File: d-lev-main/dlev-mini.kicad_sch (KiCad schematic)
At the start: 28 parts, among them J1 IO_BOARD, J3 S8B-PH-SM4-TB, J4 S8B-PH-SM4-TB, J6 S6B-PH-SM4-TB, Q1 MMBT3904, U2 AMS1117-3.3

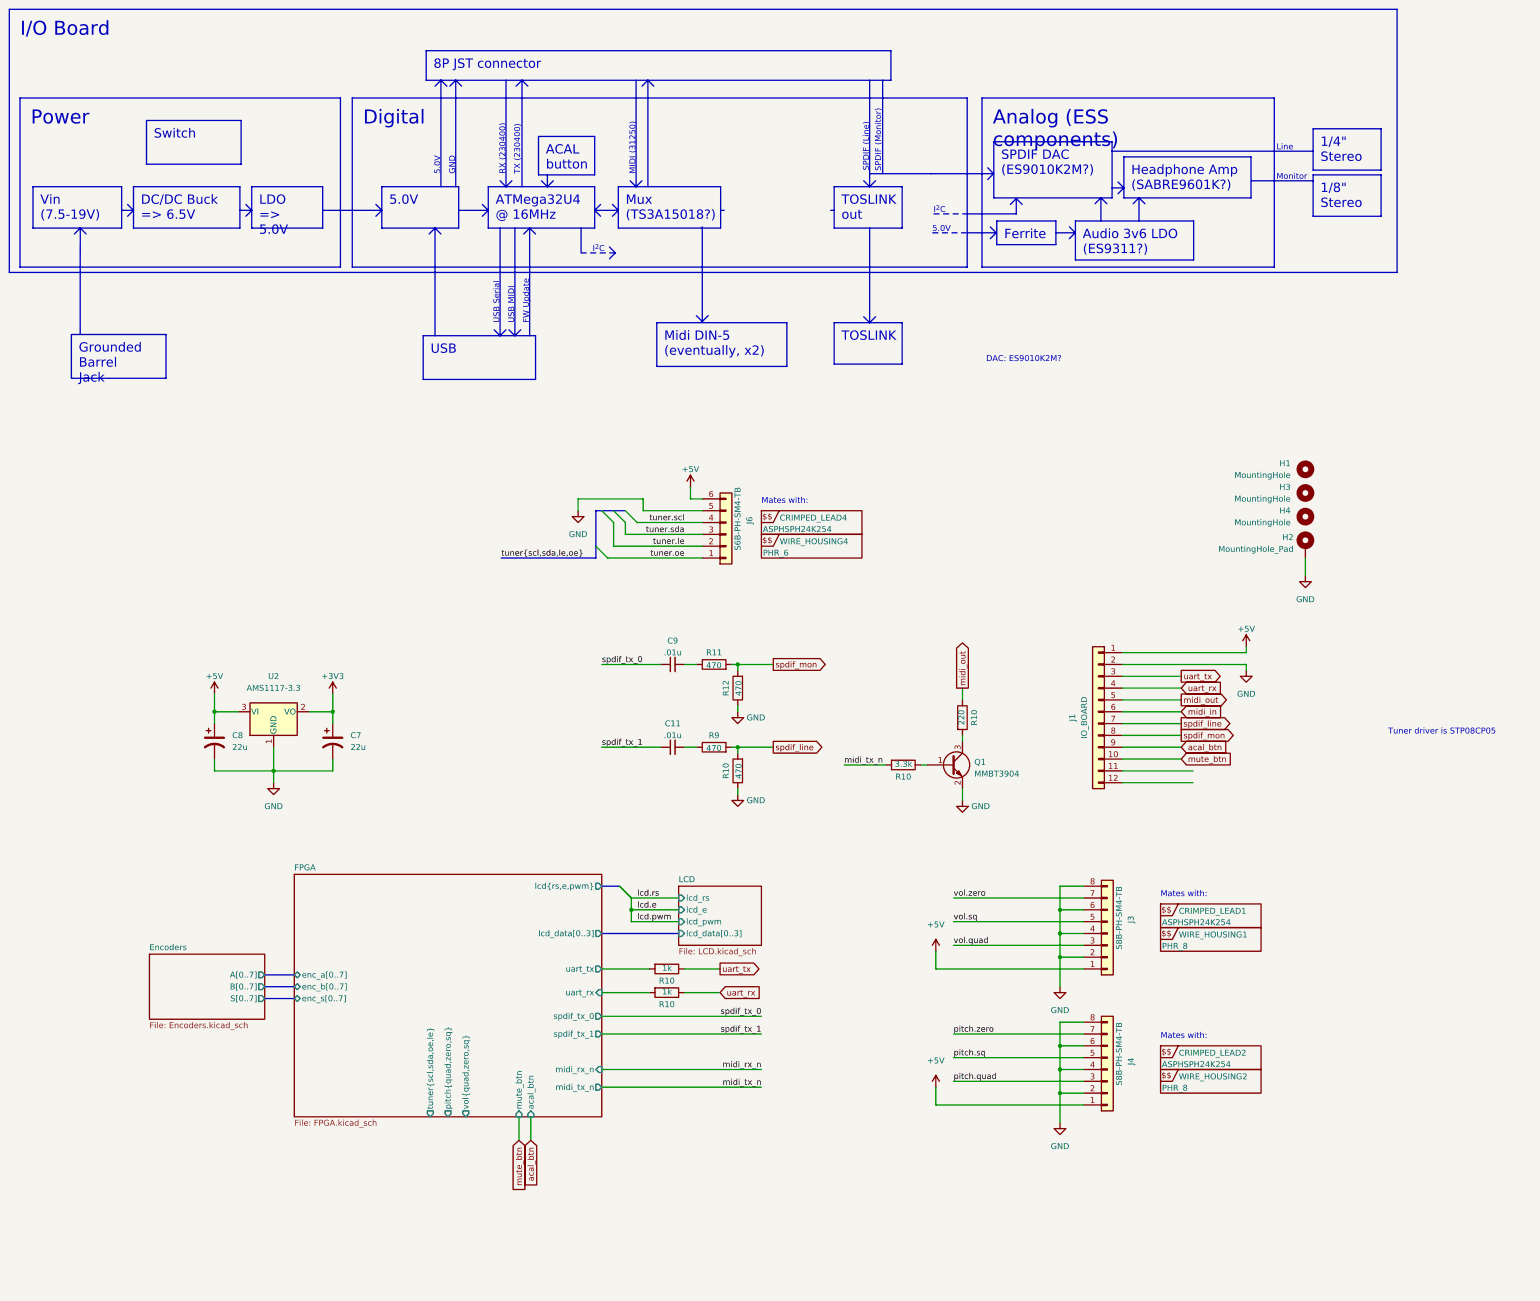
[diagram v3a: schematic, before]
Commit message: clean up 3d models
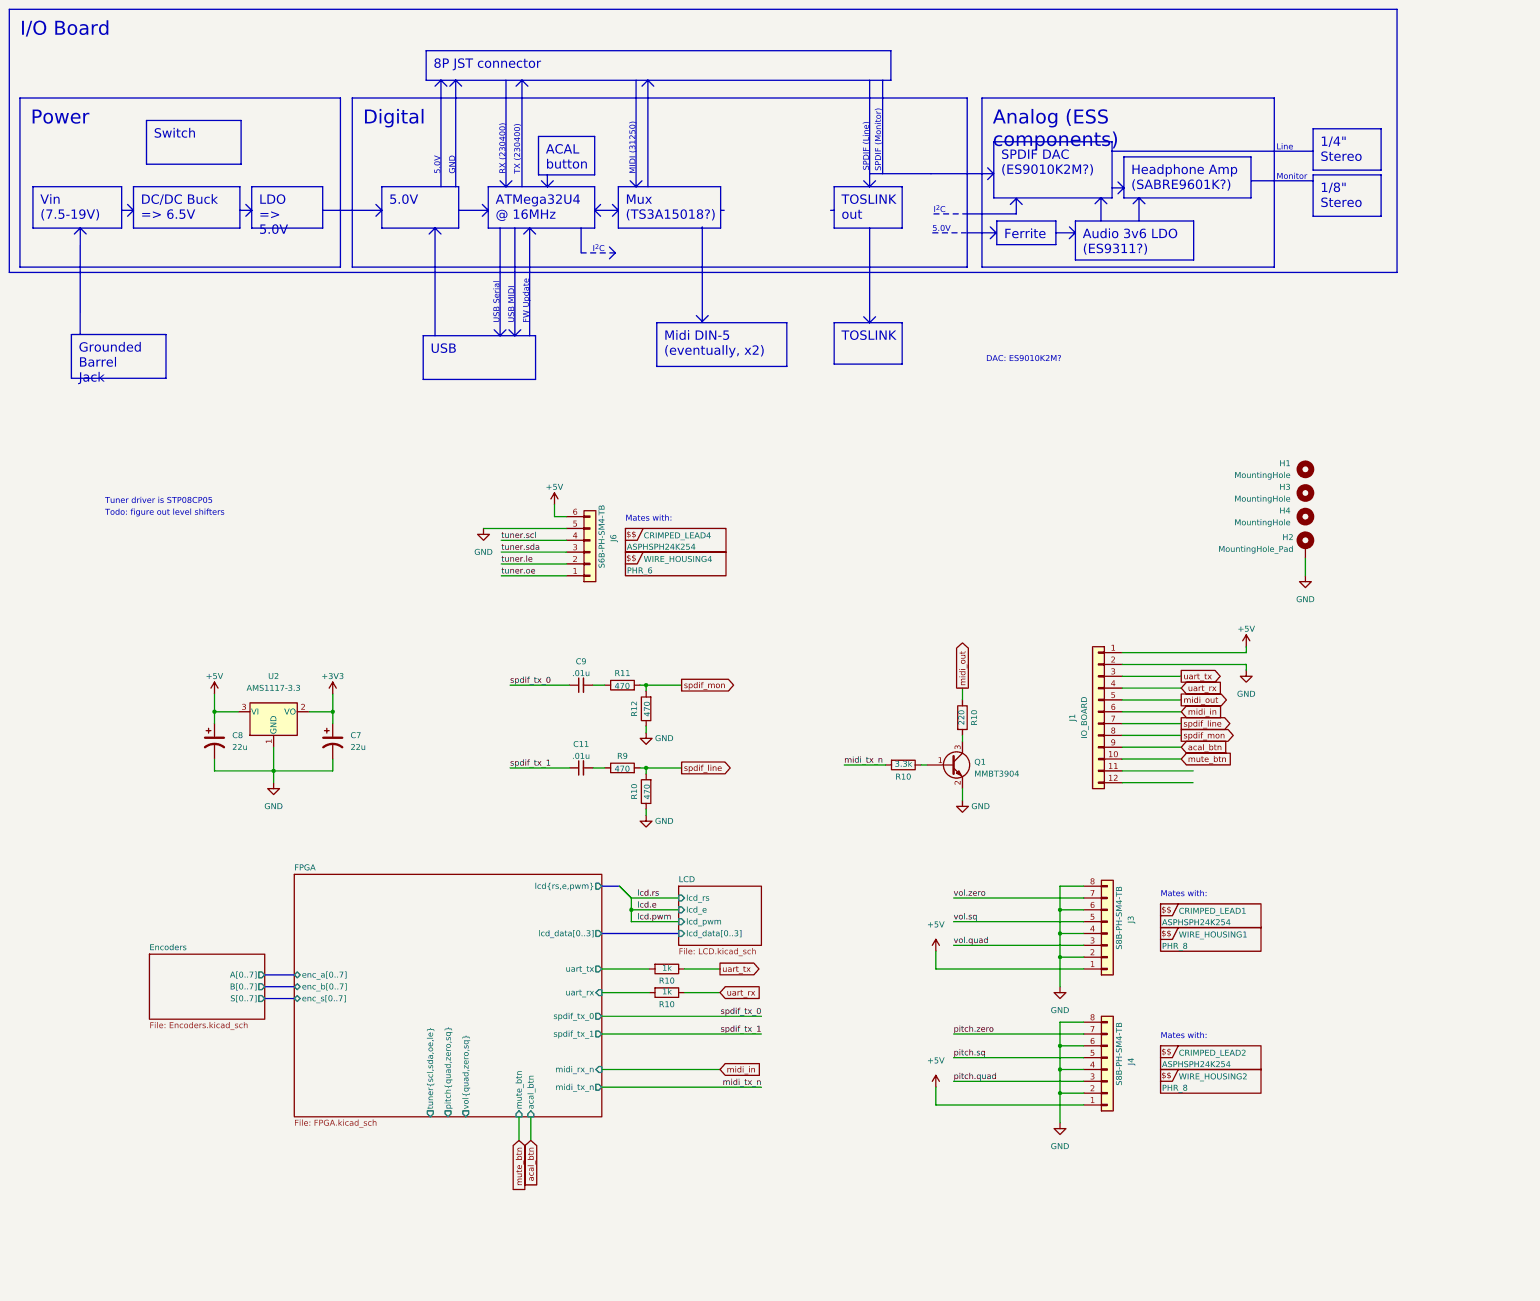
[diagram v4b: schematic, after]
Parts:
- H1, H2: footprint (none) -> d-lev:SMTSO-M4
- J1: footprint (none) -> d-lev:JST_PH_S12B-PH-SM4-TB_1x12-1MP_P2.00mm_Horizontal
- J3, J4: footprint Connector_JST:JST_PH_S8B-PH-SM4-TB_1x08-1MP_P2.00mm_Horizontal -> d-lev:JST_PH_S8B-PH-SM4-TB_1x08-1MP_P2.00mm_Horizontal
- J6: footprint Connector_JST:JST_PH_S6B-PH-SM4-TB_1x06-1MP_P2.00mm_Horizontal -> d-lev:JST_PH_S6B-PH-SM4-TB_1x06-1MP_P2.00mm_Horizontal
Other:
- note added: "Todo: figure out level shifters"
- moved on the sheet: C11, C9, CRIMPED_LEAD4, J6, R10, R11, R12, R9, WIRE_HOUSING4

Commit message: Level shifters and rearrange encoders
* WIP: use net buses more effectively to organize encoder signals
* Add application note for level shifters
* Add level shifters for UART, change MIDI level shifter BJT to FET
* Add MIDI_HI pull-up on d-lev-io board
* Add/change some footprints
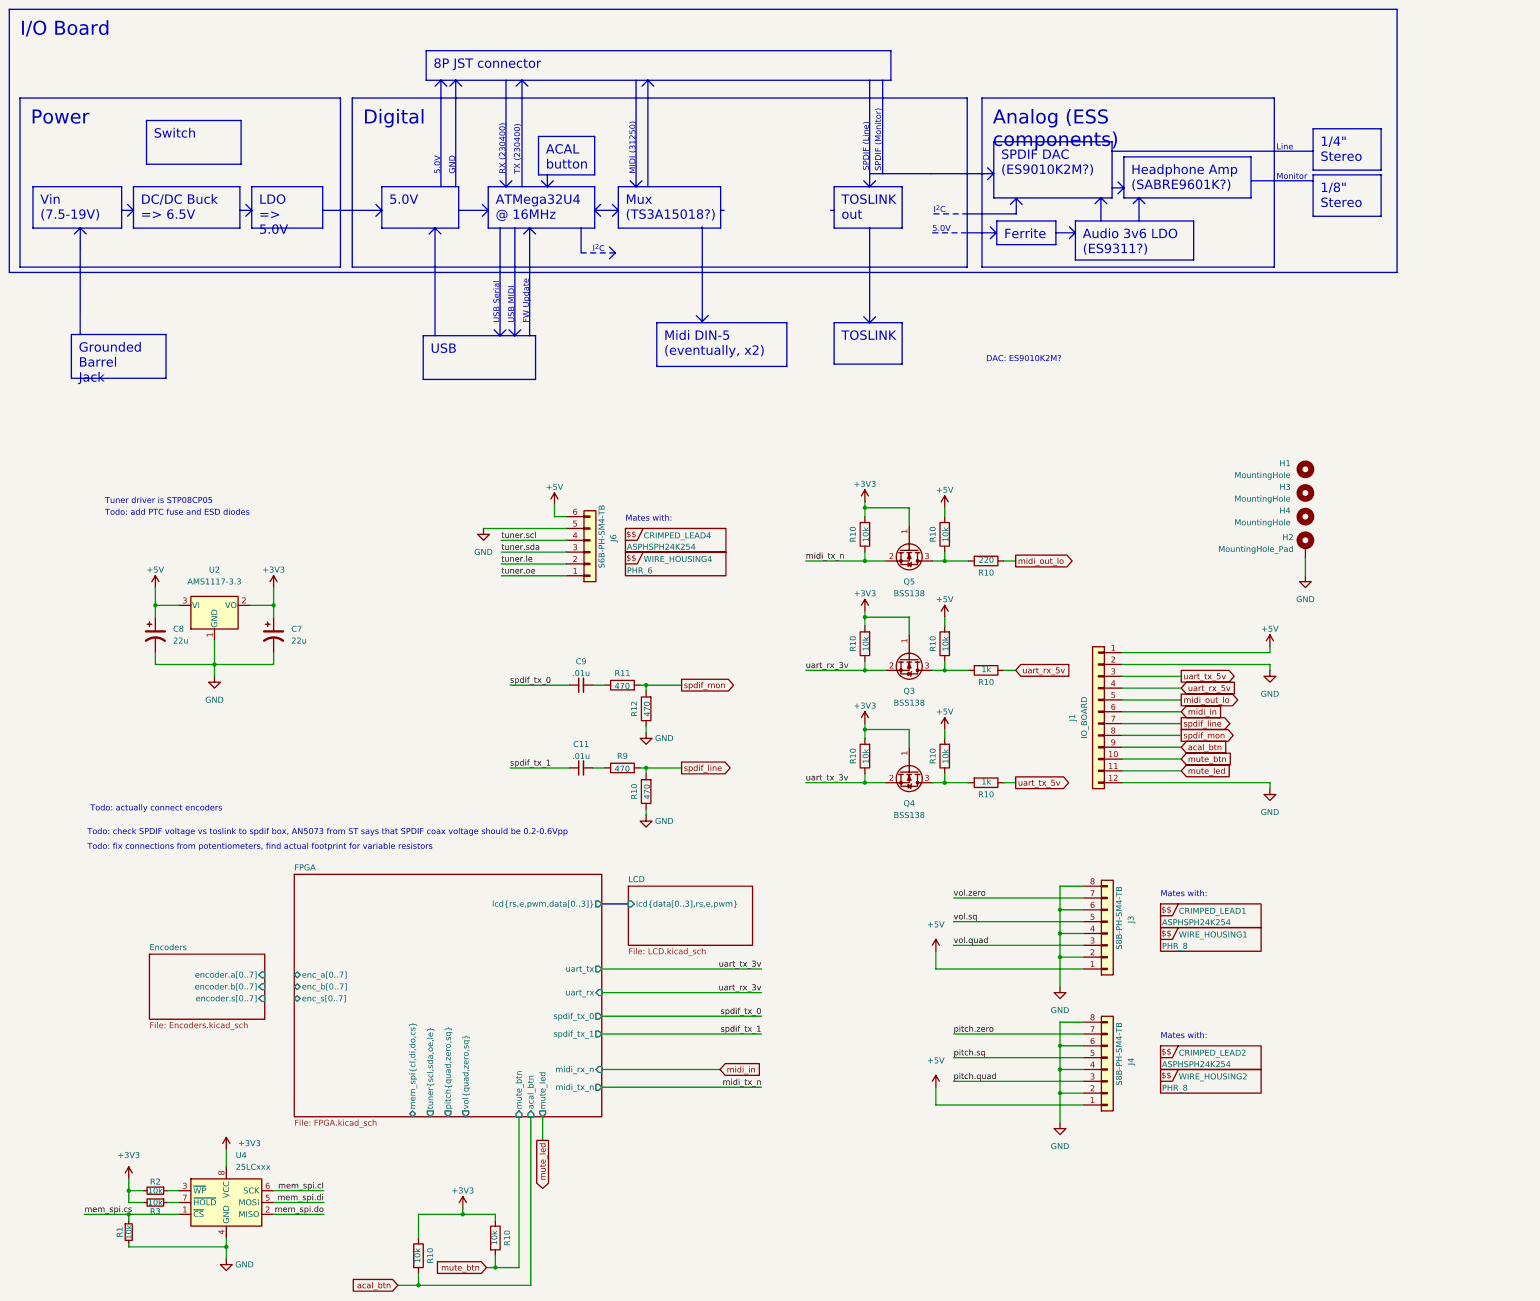
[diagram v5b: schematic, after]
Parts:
- removed Q1: MMBT3904, Package_TO_SOT_SMD:SOT-23, symbol Transistor_BJT:MMBT3904
- removed R10: 220, symbol Device:R
- removed R10: 3.3k, symbol Device:R
- removed R10 (x2): 1k, symbol Device:R
- added Q3, Q4, Q5: BSS138, Package_TO_SOT_SMD:SOT-23, symbol Transistor_FET:BSS138
- added R1, R2, R3: 10k, Resistor_SMD:R_0805_2012Metric_Pad1.20x1.40mm_HandSolder, symbol Device:R_Small
- added R10 (x2): 1k, Resistor_SMD:R_0805_2012Metric_Pad1.20x1.40mm_HandSolder, symbol Device:R
- added R10 (x8): 10k, Resistor_SMD:R_0805_2012Metric_Pad1.20x1.40mm_HandSolder, symbol Device:R
- added R10: 220, Resistor_SMD:R_0805_2012Metric_Pad1.20x1.40mm_HandSolder, symbol Device:R
- added U4: 25LCxxx, Package_SO:SOIC-8W_5.3x5.3mm_P1.27mm, symbol Memory_EEPROM:25LCxxx
- C11, C7, C8, C9: footprint (none) -> Capacitor_SMD:C_0805_2012Metric_Pad1.18x1.45mm_HandSolder
- R10, R11, R12, R9: footprint (none) -> Resistor_SMD:R_0805_2012Metric_Pad1.20x1.40mm_HandSolder
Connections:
- net +3V3: now also Q3.1 (G), Q4.1 (G), Q5.1 (G), R10.1, R10.1, R10.2, R10.2, R10.2, R2.2, R3.2, U4.8 (VCC)
- net +5V: now also R10.2, R10.2, R10.2
- net GND: now also J1.12 (Pin_12), R1.2, U4.4 (GND)
- net acal_btn: now also R10.2
- net midi_tx_n: now also Q5.2 (S), R10.1
- net mute_btn: now also R10.2
- net mute_led: now reaches J1.11 (Pin_11)
- net midi_out renamed midi_out_lo
- net midi_out_lo: now also R10.1
- net uart_rx renamed uart_rx_5v
- net uart_rx_5v: now also R10.1
- net uart_tx renamed uart_tx_5v
- net uart_tx_5v: now also R10.1
- new net: Q3.3 (D), R10.1, R10.2
- new net: Q5.3 (D), R10.1, R10.2
- new net: R3.1, U4.7 (~{HOLD})
- new net: R2.1, U4.3 (~{WP})
- new net: Q4.3 (D), R10.1, R10.2
- new net mem_spi.cl: U4.6 (SCK)
- new net mem_spi.cs: R1.1, U4.1 (~{CS})
- new net mem_spi.di: U4.5 (MOSI)
- new net mem_spi.do: U4.2 (MISO)
- new net uart_rx_3v: Q3.2 (S), R10.1
- new net uart_tx_3v: Q4.2 (S), R10.1
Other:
- sheet Encoders ports: added encoder.a[0..7], encoder.b[0..7], encoder.s[0..7]; removed A[0..7], B[0..7], S[0..7]
- sheet FPGA ports: added lcd{rs,e,pwm,data[0..3]}, mem_spi{cl,di,do,cs}, mute_led; removed lcd_data[0..3], lcd{rs,e,pwm}
- sheet LCD ports: added lcd{data[0..3],rs,e,pwm}; removed lcd_data[0..3], lcd_e, lcd_pwm, lcd_rs
- note added: "Todo: actually connect encoders"
- note added: "Todo: add PTC fuse and ESD diodes"
- note added: "Todo: check SPDIF voltage vs toslink to spdif box, AN5073 from ST says that SPDIF coax voltage should be 0.2-0.6Vpp"
- note added: "Todo: fix connections from potentiometers, find actual footprint for variable resistors"
- note removed: "Todo: figure out level shifters"
- moved on the sheet: C7, C8, U2

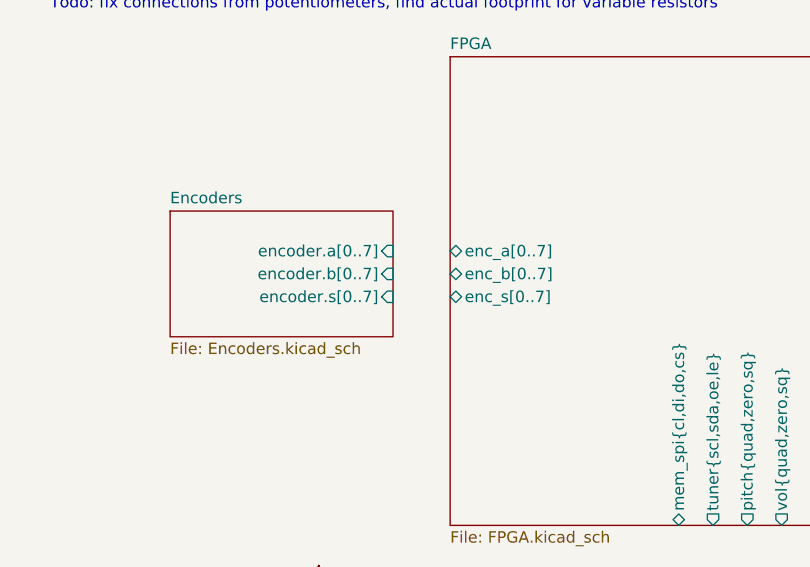
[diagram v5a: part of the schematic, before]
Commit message: more encoder bus mangling
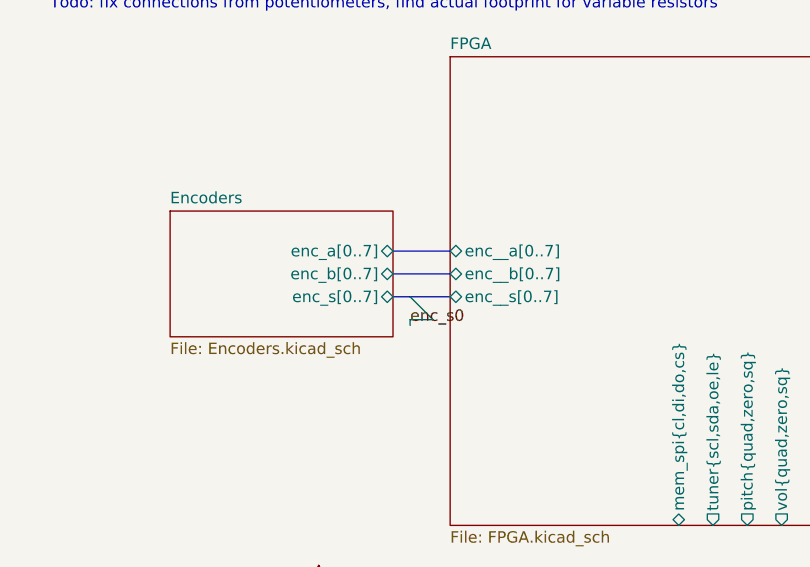
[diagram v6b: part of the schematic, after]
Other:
- sheet Encoders ports: added enc_a[0..7], enc_b[0..7], enc_s[0..7]; removed encoder.a[0..7], encoder.b[0..7], encoder.s[0..7]
- sheet FPGA ports: added enc__a[0..7], enc__b[0..7], enc__s[0..7]; removed enc_a[0..7], enc_b[0..7], enc_s[0..7]
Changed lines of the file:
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@@
   (junction (at 227.965 145.415) (diameter 0) (color 0 0 0 0)
   )
+  (bus_entry (at 59.055 130.175) (size 2.54 2.54)
+    (stroke (width 0) (type default))
+  )
   (wire (pts (xy 195.58 24.765) (xy 186.055 24.765))
     (stroke (width 0) (type default))
@@
     (stroke (width 0) (type default))
   )
+  (bus (pts (xy 57.15 127.635) (xy 63.5 127.635))
+    (stroke (width 0) (type default))
+  )
   (polyline (pts (xy 129.286 -40.386) (xy 128.016 -39.116))
     (stroke (width 0) (type default))
@@
   )
   (polyline (pts (xy 200.2282 -46.99) (xy 213.6902 -46.99))
+    (stroke (width 0) (type default))
+  )
+  (bus (pts (xy 57.15 130.175) (xy 59.055 130.175))
     (stroke (width 0) (type default))
   )
@@
     (stroke (width 0) (type default))
   )
+  (bus (pts (xy 59.055 130.175) (xy 63.5 130.175))
+    (stroke (width 0) (type default))
+  )
   (wire (pts (xy 186.055 83.82) (xy 186.055 81.915))
     (stroke (width 0) (type default))
@@
     (stroke (width 0) (type default))
   )
+  (wire (pts (xy 61.595 132.715) (xy 59.055 132.715))
+    (stroke (width 0) (type default))
+  )
   (polyline (pts (xy 114.046 -35.306) (xy 115.316 -34.036))
     (stroke (width 0) (type default))
@@
   )
   (wire (pts (xy 36.195 173.99) (xy 38.735 173.99))
+    (stroke (width 0) (type default))
+  )
+  (wire (pts (xy 59.055 132.715) (xy 59.055 133.35))
     (stroke (width 0) (type default))
   )
@@
     (stroke (width 0) (type default))
   )
+  (bus (pts (xy 57.15 125.095) (xy 63.5 125.095))
+    (stroke (width 0) (type default))
+  )
   (wire (pts (xy 227.965 106.045) (xy 233.045 106.045))
     (stroke (width 0) (type default))
@@
   )
   (label "mem_spi.cs" (at 18.415 176.53 0) (fields_autoplaced)
+    (effects (font (size 1.27 1.27)) (justify left bottom))
+  )
+  (label "enc_s0" (at 59.055 133.35 0)
     (effects (font (size 1.27 1.27)) (justify left bottom))
   )
@@
       (effects (font (size 1.27 1.27)) (justify left top))
     )
-    (pin "encoder.b[0..7]" input (at 57.15 127.635 0)
+    (pin "enc_s[0..7]" bidirectional (at 57.15 130.175 0)
       (effects (font (size 1.27 1.27)) (justify right))
     )
-    (pin "encoder.s[0..7]" input (at 57.15 130.175 0)
+    (pin "enc_a[0..7]" bidirectional (at 57.15 125.095 0)
       (effects (font (size 1.27 1.27)) (justify right))
     )
-    (pin "encoder.a[0..7]" input (at 57.15 125.095 0)
+    (pin "enc_b[0..7]" bidirectional (at 57.15 127.635 0)
       (effects (font (size 1.27 1.27)) (justify right))
     )
@@
       (effects (font (size 1.27 1.27)) (justify right))
     )
-    (pin "enc_a[0..7]" bidirectional (at 63.5 125.095 180)
-      (effects (font (size 1.27 1.27)) (justify left))
-    )
-    (pin "enc_b[0..7]" bidirectional (at 63.5 127.635 180)
-      (effects (font (size 1.27 1.27)) (justify left))
-    )
-    (pin "enc_s[0..7]" bidirectional (at 63.5 130.175 180)
-      (effects (font (size 1.27 1.27)) (justify left))
-    )
+    (pin "enc__a[0..7]" bidirectional (at 63.5 125.095 180)
+      (effects (font (size 1.27 1.27)) (justify left))
+    )
+    (pin "enc__b[0..7]" bidirectional (at 63.5 127.635 180)
+      (effects (font (size 1.27 1.27)) (justify left))
+    )
+    (pin "enc__s[0..7]" bidirectional (at 63.5 130.175 180)
+      (effects (font (size 1.27 1.27)) (justify left))
+    )
